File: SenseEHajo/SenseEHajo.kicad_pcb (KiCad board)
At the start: 2 copper layers, 141 x 56.9 mm, 81 parts, among them IC1 AP3012, IC2 MCP3221, IC3 SN74AUP1G08-Q1, IC4 K814P, J1 Conn_01x02_Male, J2 REED, J3 RTC ( DS3231), J4 Heizung, J5 Pumpe, J6 Conn_01x05, J7 L, J8 N, J9 Prog, Q1 BSS138, SW1 Reset, SW2 SW1 ( Boot ), SW3 SW2, SW4 SW3, T1 QJ8025, T2 QJ8025, U1 ESP32-WROOM-32, U2 MCP6001-OT, U3 MOC3043M, U4 MOC3043M, U5 TCA9544A, U6 LM1117-3.3

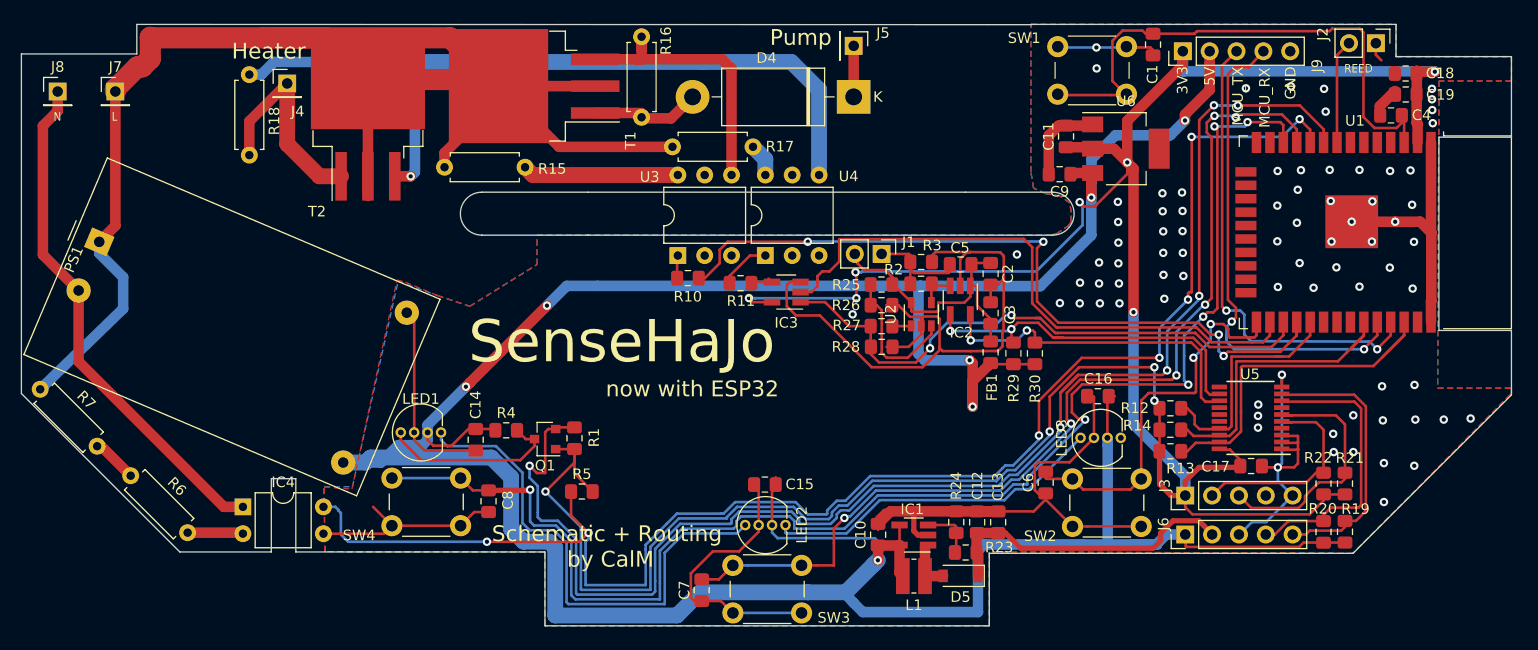
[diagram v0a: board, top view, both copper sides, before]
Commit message: Updated PCB to Revision 3
Revision 3, untested and will kill you
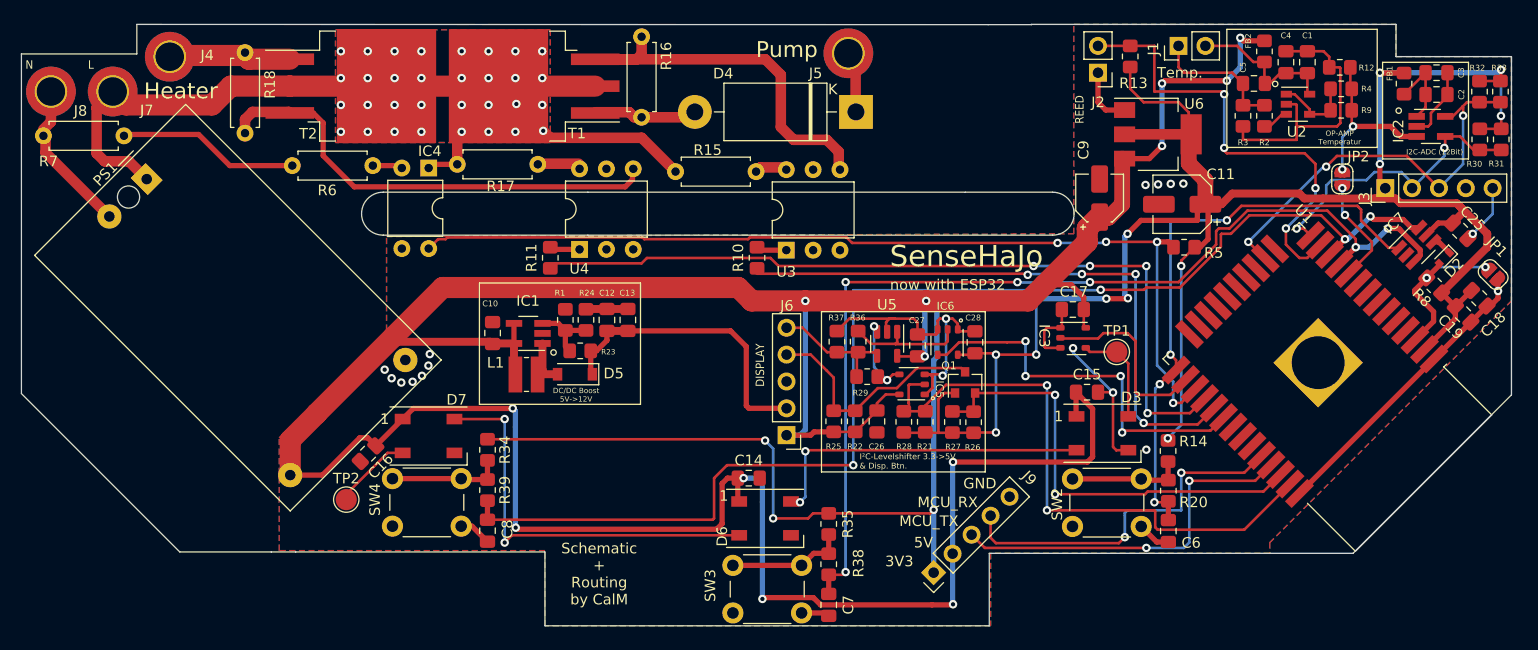
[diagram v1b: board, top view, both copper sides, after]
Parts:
- removed LED1, LED2, LED3: WS2812D, WS2812D:WS2812D_THT
- removed R19: 15k, Resistor_SMD:R_0805_2012Metric_Pad1.15x1.40mm_HandSolder
- removed SW1: Reset, Button_Switch_THT:SW_PUSH_6mm
- added C25: 100nF / 10V, Capacitor_SMD:C_0805_2012Metric_Pad1.18x1.45mm_HandSolder, F.Cu at (159.2, 39.8)
- added C26: 100nF / 10V, Capacitor_SMD:C_0805_2012Metric_Pad1.18x1.45mm_HandSolder, F.Cu at (104.1, 57.9)
- added C27: 100nF / 10V, Capacitor_SMD:C_0805_2012Metric_Pad1.18x1.45mm_HandSolder, F.Cu at (107.9, 50.7)
- added C28: 100nF / 10V, Capacitor_SMD:C_0805_2012Metric_Pad1.18x1.45mm_HandSolder, F.Cu at (113.3, 50.4)
- added D2: D_Schottky, Diode_SMD:D_SOD-523, F.Cu at (157.7, 42.4)
- added D3: WS2812B, LED_SMD:LED_WS2812B_PLCC4_5.0x5.0mm_P3.2mm, F.Cu at (125.4, 59.0)
- added D6: WS2812B, LED_SMD:LED_WS2812B_PLCC4_5.0x5.0mm_P3.2mm, F.Cu at (93.5, 67.1)
- added D7: WS2812B, LED_SMD:LED_WS2812B_PLCC4_5.0x5.0mm_P3.2mm, F.Cu at (61.6, 59.3)
- added FB2: Ferrite_Bead, Resistor_SMD:R_0805_2012Metric_Pad1.20x1.40mm_HandSolder, F.Cu at (140.7, 22.9)
- added IC5: 74LVC1G125, SC-74A_SOT753:SC-74A, F.Cu at (108.6, 55.3)
- added IC6: 74LVC1G125, SC-74A_SOT753:SC-74A, F.Cu at (111.7, 49.2)
- added IC7: 74LVC1G10, Package_TO_SOT_SMD:SOT-23-6_Handsoldering, F.Cu at (155.1, 41.2)
- added JP1: Jumper_2_Open, Jumper:SolderJumper-2_P1.3mm_Open_RoundedPad1.0x1.5mm, F.Cu at (162.4, 44.0)
- added JP2: Jumper_2_Open, Jumper:SolderJumper-2_P1.3mm_Open_RoundedPad1.0x1.5mm, F.Cu at (148.1, 34.9)
- added R31: 10k, Resistor_SMD:R_0805_2012Metric_Pad1.20x1.40mm_HandSolder, F.Cu at (163.1, 31.2)
- added R32: 10k, Resistor_SMD:R_0805_2012Metric_Pad1.20x1.40mm_HandSolder, F.Cu at (161.1, 26.7)
- added R33: 10k, Resistor_SMD:R_0805_2012Metric_Pad1.20x1.40mm_HandSolder, F.Cu at (163.0, 26.7)
- added R34: 10k, Resistor_SMD:R_0805_2012Metric_Pad1.20x1.40mm_HandSolder, F.Cu at (67.2, 60.6)
- added R35: 10k, Resistor_SMD:R_0805_2012Metric_Pad1.20x1.40mm_HandSolder, F.Cu at (99.5, 67.6)
- added R36: 10k, Resistor_SMD:R_0805_2012Metric_Pad1.20x1.40mm_HandSolder, F.Cu at (102.3, 50.3)
- added R37: 1k, Resistor_SMD:R_0805_2012Metric_Pad1.20x1.40mm_HandSolder, F.Cu at (100.3, 50.3)
- added R38: 1k, Resistor_SMD:R_0805_2012Metric_Pad1.20x1.40mm_HandSolder, F.Cu at (99.5, 71.4)
- added R39: 1k, Resistor_SMD:R_0805_2012Metric_Pad1.20x1.40mm_HandSolder, F.Cu at (67.2, 64.4)
- added R8: 10k, Resistor_SMD:R_0805_2012Metric_Pad1.20x1.40mm_HandSolder, F.Cu at (156.8, 45.0)
- added R9: 10k, Resistor_SMD:R_0805_2012Metric_Pad1.20x1.40mm_HandSolder, F.Cu at (148.0, 28.4)
- added REF**: MountingHole_2.1mm, MountingHole:MountingHole_2.1mm, F.Cu at (33.2, 36.7)
- added TP1: TestPoint, TestPoint:TestPoint_Pad_D2.0mm, F.Cu at (126.7, 51.3)
- added TP2: TestPoint, TestPoint:TestPoint_Pad_D2.0mm, F.Cu at (53.8, 65.3)
- C1: value 100nF / 25V -> 1uF / 10V; footprint Capacitor_SMD:C_0805_2012Metric_Pad1.15x1.40mm_HandSolder -> Capacitor_SMD:C_0805_2012Metric_Pad1.18x1.45mm_HandSolder
- C10, C12, C13, C2, C3, C5: footprint Capacitor_SMD:C_0805_2012Metric_Pad1.15x1.40mm_HandSolder -> Capacitor_SMD:C_0805_2012Metric_Pad1.18x1.45mm_HandSolder
- C11: value 100uF -> 47uF/10V; footprint Capacitor_SMD:C_0805_2012Metric_Pad1.15x1.40mm_HandSolder -> Capacitor_SMD:CP_Elec_5x5.3
- C14, C15, C16, C17, C19, C7, C8: value 100nF -> 100nF / 10V; footprint Capacitor_SMD:C_0805_2012Metric_Pad1.15x1.40mm_HandSolder -> Capacitor_SMD:C_0805_2012Metric_Pad1.18x1.45mm_HandSolder
- C18: value 10uF -> 10uF / 10V; footprint Capacitor_SMD:C_0805_2012Metric_Pad1.15x1.40mm_HandSolder -> Capacitor_SMD:C_0805_2012Metric_Pad1.18x1.45mm_HandSolder
- C4: value 10uF / 25V -> 100nF / 10V; footprint Capacitor_SMD:C_0805_2012Metric_Pad1.15x1.40mm_HandSolder -> Capacitor_SMD:C_0805_2012Metric_Pad1.18x1.45mm_HandSolder
- C6: value 100nF / 25V -> 100nF / 10V; footprint Capacitor_SMD:C_0805_2012Metric_Pad1.15x1.40mm_HandSolder -> Capacitor_SMD:C_0805_2012Metric_Pad1.18x1.45mm_HandSolder
- C9: value 10uF -> 10uF/10V; footprint Capacitor_SMD:C_0805_2012Metric_Pad1.15x1.40mm_HandSolder -> Capacitor_SMD:CP_Elec_4x4.5
- FB1: footprint Capacitor_SMD:C_0805_2012Metric_Pad1.15x1.40mm_HandSolder -> Resistor_SMD:R_0805_2012Metric_Pad1.20x1.40mm_HandSolder
- IC3: value SN74AUP1G08-Q1 -> 74LVC1G125; footprint Package_TO_SOT_SMD:SOT-23-5_HandSoldering -> SC-74A_SOT753:SC-74A
- J4: value Heizung -> Heizung L; footprint Connector_PinHeader_2.54mm:PinHeader_1x01_P2.54mm_Vertical -> MountingHole:MountingHole_2.7mm_M2.5_DIN965_Pad_TopBottom
- J5: value Pumpe -> Pumpe L; footprint Connector_PinHeader_2.54mm:PinHeader_1x01_P2.54mm_Vertical -> MountingHole:MountingHole_2.7mm_M2.5_DIN965_Pad_TopBottom
- J7, J8: footprint Connector_PinHeader_2.54mm:PinHeader_1x01_P2.54mm_Vertical -> MountingHole:MountingHole_2.7mm_M2.5_DIN965_Pad_TopBottom
- R1, R10, R11, R2, R3, R5: footprint Resistor_SMD:R_0805_2012Metric_Pad1.15x1.40mm_HandSolder -> Resistor_SMD:R_0805_2012Metric_Pad1.20x1.40mm_HandSolder
- R12, R24: value 4k7 -> 10k; footprint Resistor_SMD:R_0805_2012Metric_Pad1.15x1.40mm_HandSolder -> Resistor_SMD:R_0805_2012Metric_Pad1.20x1.40mm_HandSolder
- R13, R14, R21, R22, R30: value 2k2 -> 10k; footprint Resistor_SMD:R_0805_2012Metric_Pad1.15x1.40mm_HandSolder -> Resistor_SMD:R_0805_2012Metric_Pad1.20x1.40mm_HandSolder
- R20: value 15k -> 1k; footprint Resistor_SMD:R_0805_2012Metric_Pad1.15x1.40mm_HandSolder -> Resistor_SMD:R_0805_2012Metric_Pad1.20x1.40mm_HandSolder
- R23: value 39k -> 43.2k; footprint Resistor_SMD:R_0805_2012Metric_Pad1.15x1.40mm_HandSolder -> Resistor_SMD:R_0805_2012Metric_Pad1.20x1.40mm_HandSolder
- R25: value 1k -> 10k; footprint Resistor_SMD:R_0805_2012Metric_Pad1.15x1.40mm_HandSolder -> Resistor_SMD:R_0805_2012Metric_Pad1.20x1.40mm_HandSolder
- R26: value 3k9 -> 10k; footprint Resistor_SMD:R_0805_2012Metric_Pad1.15x1.40mm_HandSolder -> Resistor_SMD:R_0805_2012Metric_Pad1.20x1.40mm_HandSolder
- R27: value 1k8 -> 10k; footprint Resistor_SMD:R_0805_2012Metric_Pad1.15x1.40mm_HandSolder -> Resistor_SMD:R_0805_2012Metric_Pad1.20x1.40mm_HandSolder
- R28: value 3k3 -> 10k; footprint Resistor_SMD:R_0805_2012Metric_Pad1.15x1.40mm_HandSolder -> Resistor_SMD:R_0805_2012Metric_Pad1.20x1.40mm_HandSolder
- R29: value 2k2 -> 100R; footprint Resistor_SMD:R_0805_2012Metric_Pad1.15x1.40mm_HandSolder -> Resistor_SMD:R_0805_2012Metric_Pad1.20x1.40mm_HandSolder
- R4: value 10k -> 10k (DNP); footprint Resistor_SMD:R_0805_2012Metric_Pad1.15x1.40mm_HandSolder -> Resistor_SMD:R_0805_2012Metric_Pad1.20x1.40mm_HandSolder
- SW3: value SW2 -> MACHINE_SW2
- SW4: value SW3 -> MACHINE_SW3
- U1: footprint RF_Module:ESP32-WROOM-32 -> ESP32_Handsolder:ESP32-WROOM-32_HandSolder
- U5: value TCA9544A -> MCP6001-OT; footprint Package_SO:TSSOP-20_4.4x6.5mm_P0.65mm -> Package_TO_SOT_SMD:SOT-23-5
- U6: footprint Package_TO_SOT_SMD:SOT-223 -> Package_TO_SOT_SMD:SOT-223-3_TabPin2
- moved R4 85.3 mm to (148.0, 26.4), turned to 180 degrees
- moved C16 69.3 mm to (55.9, 60.9), turned to -135 degrees
- moved R5 61.5 mm to (133.1, 41.4)
- moved J9 54.7 mm to (109.4, 72.2), turned to 135 degrees
- moved C3 47.9 mm to (157.0, 24.9), turned to 0 degrees
- moved IC2 47.5 mm to (156.5, 30.0), turned to 0 degrees
- moved R30 46.7 mm to (161.1, 31.2)
- moved FB1 46.6 mm to (153.9, 25.9), turned to -90 degrees
- moved C2 45.5 mm to (157.0, 27.0), turned to 0 degrees
- moved R22 44.7 mm to (102.0, 57.9), turned to -90 degrees
- moved L1 41.3 mm to (70.9, 53.4)
- moved C10 41.2 mm to (67.7, 49.5)
- moved D5 41.2 mm to (75.5, 53.4)
- moved R23 41.2 mm to (76.0, 51.2)
- moved IC1 41.2 mm to (71.1, 49.6)
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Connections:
- C17 pad 2: +3V3 -> +5V
- C5 pad 1: Net-(C2-Pad1) -> Net-(C1-Pad1)
- C6 pad 2: Net-(C6-Pad2) -> SW1
- C7 pad 2: Net-(C7-Pad2) -> SW2
- C8 pad 2: Net-(C8-Pad2) -> SW3
- FB1 pad 1: +5V -> +3V3
- IC2 pad 4: SDA_ADC -> SDA_3V3
- IC2 pad 5: SCL_ADC -> SCL_3V3
- IC3 pad 1: ~{OVERTEMP} -> GND
- IC3 pad 2: Heizung -> WS2812_3V3
- IC3 pad 4: Net-(IC3-Pad4) -> Net-(D3-Pad4)
- IC3 pad 5: +3V3 -> +5V
- IC4 pad 1: N_230V -> L_230V
- IC4 pad 4: IO25 -> MAINS_HALVEWAVES
- J1 pad 2: Net-(C2-Pad1) -> Net-(C1-Pad1)
- J2 pad 2: REED -> REED_IN
- J3 pad 2: SDA_RTC -> SDA_3V3
- J3 pad 3: SCL_RTC -> SCL_3V3
- J3 pad 4: Net-(J3-Pad4) -> unconnected-(J3-Pad4)
- Q1 pad 2: WS2812_3V3 -> I2C_DSP_SDA
- Q1 pad 3: Net-(LED1-Pad4) -> SDA_DSP
- R1 pad 1: +3V3 -> Net-(IC1-Pad3)
- R1 pad 2: WS2812_3V3 -> GND
- R10 pad 2: Pumpe -> PUMP_MOC
- R11 pad 2: Net-(IC3-Pad4) -> Heizung_MOC
- R12 pad 1: +3V3 -> Net-(IC2-Pad3)
- R12 pad 2: I2C_INT -> GND
- R13 pad 2: I2C_SCL -> REED_IN
- R14 pad 2: I2C_SDA -> Net-(R14-Pad2)
- R2 pad 2: Net-(IC2-Pad3) -> Net-(R2-Pad2)
- R20 pad 1: +5V -> Net-(R14-Pad2)
- R20 pad 2: SDA_DSP -> SW1
- R21 pad 1: +3V3 -> I2C_DSP_SCL
- R21 pad 2: SCL_RTC -> +3V3
- R22 pad 1: +3V3 -> SDA_DSP
- R22 pad 2: SDA_RTC -> +5V
- R25 pad 1: Net-(C2-Pad1) -> +5V
- R25 pad 2: Net-(R25-Pad2) -> SDA_DSP
- R26 pad 1: Net-(R25-Pad2) -> I2C_DSP_SDA
- R26 pad 2: GND -> +3V3
- R27 pad 1: ~{OVERTEMP} -> +3V3
- R27 pad 2: Net-(R27-Pad2) -> I2C_DSP_SDA
- R28 pad 1: ~{OVERTEMP} -> +3V3
- R28 pad 2: GND -> I2C_DSP_SCL
- R29 pad 1: +5V -> SCL_DSP
- R29 pad 2: SDA_ADC -> Net-(IC5-Pad4)
- R30 pad 1: +5V -> SDA_3V3
- R30 pad 2: SCL_ADC -> +3V3
- R4 pad 1: +5V -> Net-(IC2-Pad3)
- R4 pad 2: Net-(LED1-Pad4) -> Net-(R4-Pad2)
- R5 pad 1: IO25 -> MAINS_HALVEWAVES
- R7 pad 1: L_230V -> N_230V
- SW2 pad 1: Net-(C6-Pad2) -> Net-(R14-Pad2)
- SW3 pad 1: Net-(C7-Pad2) -> Net-(R35-Pad2)
- SW4 pad 1: Net-(C8-Pad2) -> Net-(R34-Pad2)
- U1 pad 10: IO25 -> ESP32_ADC
- U1 pad 11: Net-(C7-Pad2) -> SW2
- U1 pad 12: Net-(C8-Pad2) -> SW3
- U1 pad 13: IO14 -> REED_IN
- U1 pad 14: IO12 -> SDA_3V3
- U1 pad 16: IO13 -> SCL_3V3
- U1 pad 17: Net-(U1-Pad17) -> unconnected-(U1-Pad17)
- U1 pad 18: Net-(U1-Pad18) -> unconnected-(U1-Pad18)
- U1 pad 19: Net-(U1-Pad19) -> unconnected-(U1-Pad19)
- U1 pad 20: Net-(U1-Pad20) -> unconnected-(U1-Pad20)
- U1 pad 21: Net-(U1-Pad21) -> unconnected-(U1-Pad21)
- U1 pad 22: Net-(U1-Pad22) -> unconnected-(U1-Pad22)
- U1 pad 23: IO15 -> unconnected-(U1-Pad23)
- U1 pad 24: IO2 -> unconnected-(U1-Pad24)
- U1 pad 25: Net-(C6-Pad2) -> SW1
- U1 pad 26: Heizung -> WS2812_3V3
- U1 pad 27: ~{OVERTEMP} -> MAINS_HALVEWAVES
- U1 pad 28: Pumpe -> Heizung_MOC
- U1 pad 29: I2C_INT -> PUMP_MOC
- U1 pad 3: Net-(C1-Pad1) -> Net-(D2-Pad2)
- U1 pad 30: IO18 -> DISP_BTN
- U1 pad 31: IO19 -> unconnected-(U1-Pad31)
- U1 pad 32: Net-(U1-Pad32) -> unconnected-(U1-Pad32)
- U1 pad 33: I2C_SDA -> unconnected-(U1-Pad33)
- U1 pad 36: I2C_SCL -> I2C_DSP_SDA
- U1 pad 37: IO23 -> I2C_DSP_SCL
- U1 pad 4: SVP -> unconnected-(U1-Pad4)
- U1 pad 5: SVN -> unconnected-(U1-Pad5)
- U1 pad 6: IO34 -> unconnected-(U1-Pad6)
- U1 pad 7: IO35 -> unconnected-(U1-Pad7)
- U1 pad 8: REED -> unconnected-(U1-Pad8)
- U1 pad 9: WS2812_3V3 -> unconnected-(U1-Pad9)
- U2 pad 1: Net-(R27-Pad2) -> Net-(R4-Pad2)
- U2 pad 3: Net-(R25-Pad2) -> Net-(R2-Pad2)
- U2 pad 4: Net-(IC2-Pad3) -> Net-(R4-Pad2)
- U2 pad 5: Net-(C2-Pad1) -> Net-(C1-Pad1)
- U3 pad 3: Net-(U3-Pad3) -> unconnected-(U3-Pad3)
- U3 pad 5: Net-(U3-Pad5) -> unconnected-(U3-Pad5)
- U4 pad 3: Net-(U4-Pad3) -> unconnected-(U4-Pad3)
- U4 pad 5: Net-(U4-Pad5) -> unconnected-(U4-Pad5)
- U5 pad 1: GND -> Net-(IC6-Pad2)
- U5 pad 3: GND -> Net-(IC5-Pad4)
- U5 pad 4: Net-(U5-Pad4) -> SCL_DSP
- U5 pad 5: SDA_RTC -> +5V
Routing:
- net IO25: track 142.3 -> 0.00 mm, vias 7 -> 0
- net Net-(C8-Pad2): track 137.7 -> 0.00 mm, vias 6 -> 0
- net GND: track 266.3 -> 135.1 mm, vias 78 -> 18
- net SW3: track 0.00 -> 118.8 mm, vias 0 -> 4
- net WS2812_3V3: track 136.2 -> 17.9 mm, vias 6 -> 0
- net SW2: track 0.00 -> 96.0 mm, vias 0 -> 6
- net Net-(C7-Pad2): track 94.2 -> 0.00 mm, vias 6 -> 0
- net MAINS_HALVEWAVES: track 0.00 -> 90.0 mm, vias 0 -> 4
- net Heizung_MOC: track 0.00 -> 77.0 mm, vias 0 -> 4
- net L_230V: track 159.4 -> 83.0 mm, vias 0 -> 32
- net Pumpe: track 71.8 -> 0.00 mm, vias 4 -> 0
- net PUMP_MOC: track 0.00 -> 57.6 mm, vias 0 -> 4
- net I2C_DSP_SCL: track 0.00 -> 57.4 mm, vias 0 -> 2
- net Heizung: track 57.1 -> 0.00 mm
- net ~{OVERTEMP}: track 55.4 -> 0.00 mm, vias 2 -> 0
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- added copper zone on B.Cu, net L_230V
- added copper zone on F.Cu, net L_230V
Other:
- outline, holes or cut-outs redrawn
- rule pad_to_mask_clearance: 0.051 -> 0
- board text added: "DC/DC Boost 5V->12V"
- board text added: "I2C-ADC (12Bit)"
- board text added: "I²C-Levelshifter 3.3->5V & Disp. Btn."
- board text added: "OP-AMP Temperatur"
- board text added: "Temp."
